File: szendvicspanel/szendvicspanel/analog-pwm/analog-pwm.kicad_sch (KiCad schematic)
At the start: 24 parts, among them J3 Conn_01x04_Pin, U1 TL072, U2 TL072

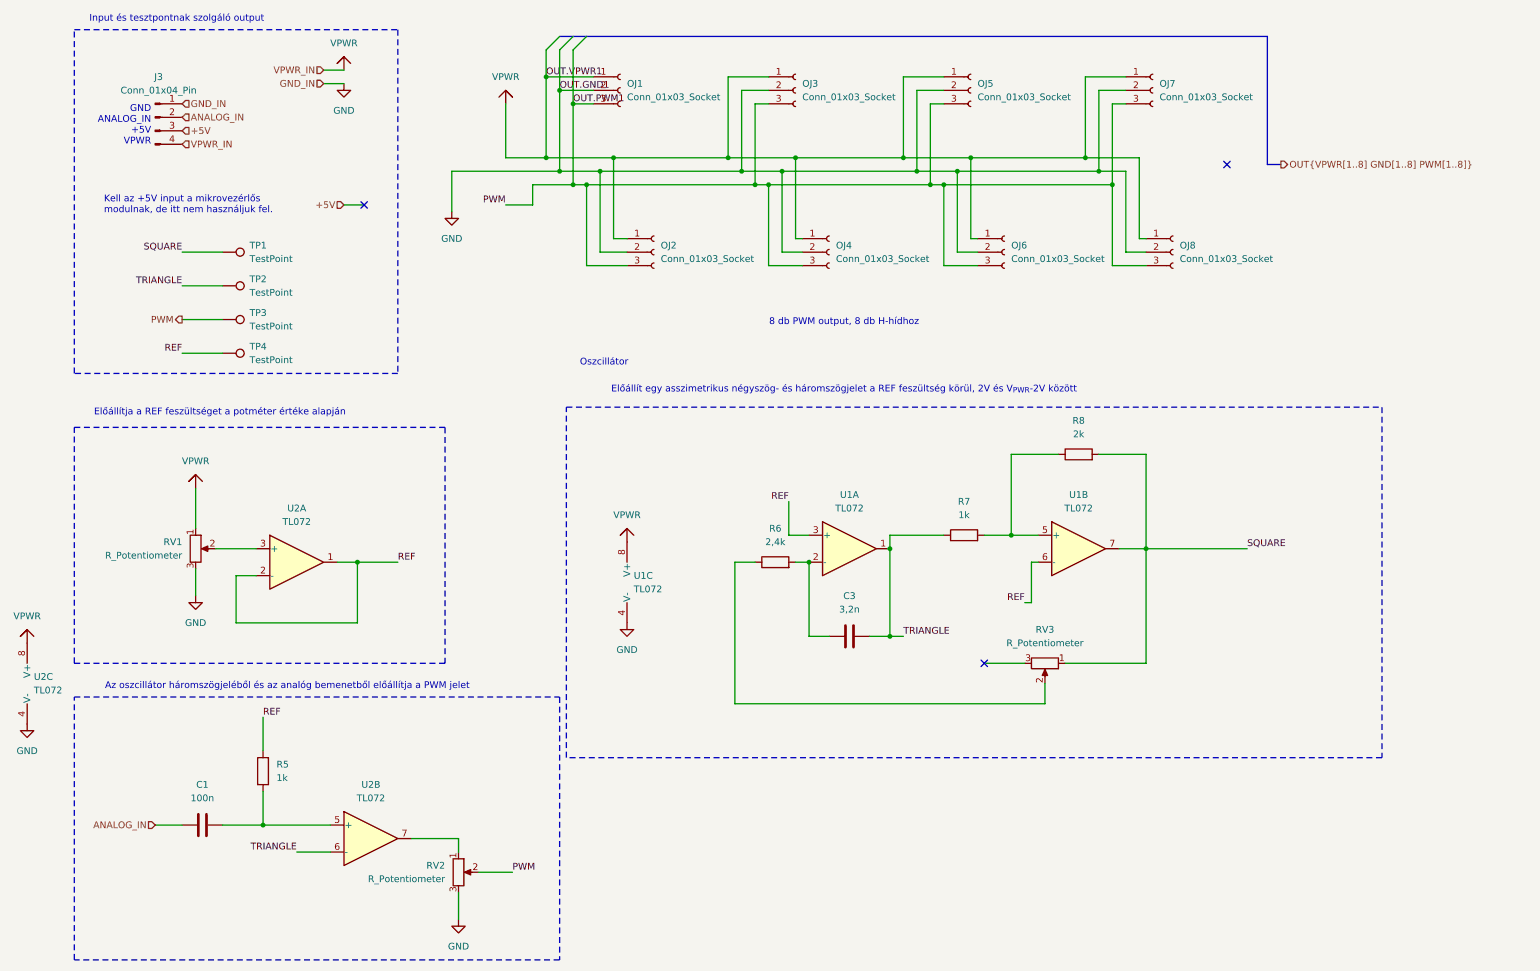
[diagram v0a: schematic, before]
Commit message: Átstrukturálás hierarchikus PCB-hez
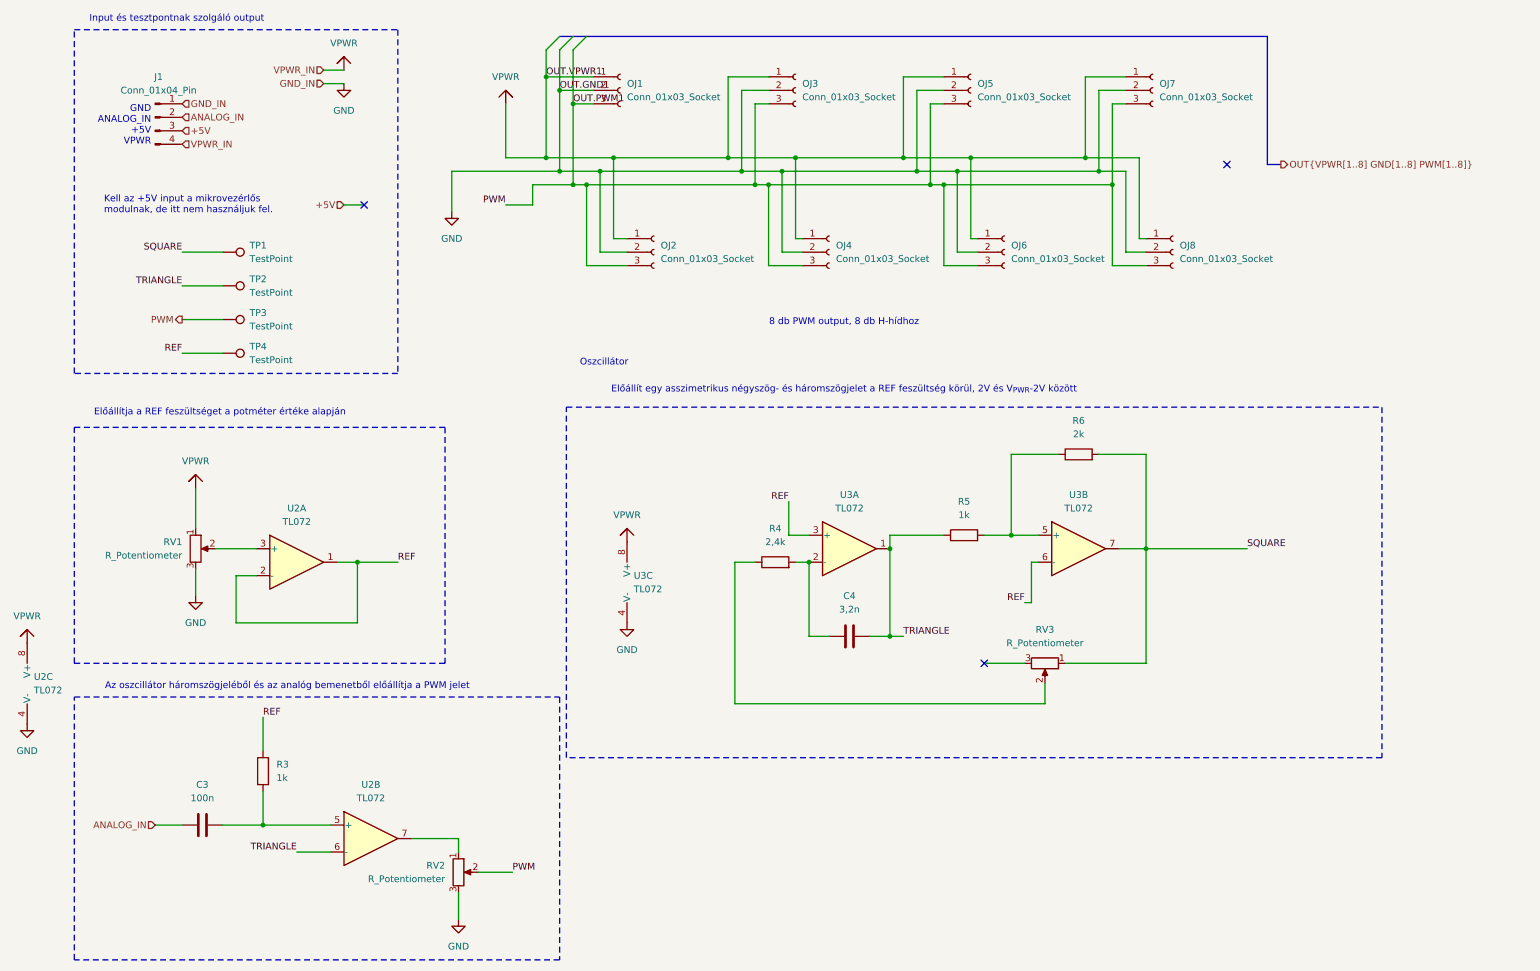
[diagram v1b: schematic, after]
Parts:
- renumbered C1 to C3, C3 to C4, J3 to J1, R5 to R3, R6 to R4, R7 to R5, R8 to R6, U1 to U3
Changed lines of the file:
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@@
 		(dnp no)
 		(fields_autoplaced yes)
-		(property "Reference" "#VPWR06"
+		(property "Reference" "#VPWR03"
 			(at 81.28 30.48 0)
 			(effects
@@
 			(project "szendvicspanel"
 				(path "/2e536be4-7a69-4064-ab31-c73232c2dcfe/2931c1ad-d139-4f81-b248-365d50218096"
-					(reference "#VPWR06")
+					(reference "#VPWR03")
 					(unit 1)
 				)
@@
 		(dnp no)
 		(fields_autoplaced yes)
-		(property "Reference" "R7"
+		(property "Reference" "R5"
 			(at 198.12 111.76 90)
 			(effects
@@
 			(project "szendvicspanel"
 				(path "/2e536be4-7a69-4064-ab31-c73232c2dcfe/2931c1ad-d139-4f81-b248-365d50218096"
-					(reference "R7")
+					(reference "R5")
 					(unit 1)
 				)
@@
 		(dnp no)
 		(fields_autoplaced yes)
-		(property "Reference" "R6"
+		(property "Reference" "R4"
 			(at 162.56 116.84 90)
 			(effects
@@
 			(project "szendvicspanel"
 				(path "/2e536be4-7a69-4064-ab31-c73232c2dcfe/2931c1ad-d139-4f81-b248-365d50218096"
-					(reference "R6")
+					(reference "R4")
 					(unit 1)
 				)
@@
 		(dnp no)
 		(fields_autoplaced yes)
-		(property "Reference" "#PWR08"
+		(property "Reference" "#PWR012"
 			(at 21.59 160.02 0)
 			(effects
@@
 			(project "szendvicspanel"
 				(path "/2e536be4-7a69-4064-ab31-c73232c2dcfe/2931c1ad-d139-4f81-b248-365d50218096"
-					(reference "#PWR08")
+					(reference "#PWR012")
 					(unit 1)
 				)
@@
 		(dnp no)
 		(fields_autoplaced yes)
-		(property "Reference" "U1"
+		(property "Reference" "U3"
 			(at 219.71 110.49 0)
 			(effects
@@
 			(project ""
 				(path "/2e536be4-7a69-4064-ab31-c73232c2dcfe/2931c1ad-d139-4f81-b248-365d50218096"
-					(reference "U1")
+					(reference "U3")
 					(unit 2)
 				)
@@
 		(dnp no)
 		(fields_autoplaced yes)
-		(property "Reference" "C3"
+		(property "Reference" "C4"
 			(at 176.53 129.54 90)
 			(effects
@@
 			(project "szendvicspanel"
 				(path "/2e536be4-7a69-4064-ab31-c73232c2dcfe/2931c1ad-d139-4f81-b248-365d50218096"
-					(reference "C3")
+					(reference "C4")
 					(unit 1)
 				)
@@
 		(dnp no)
 		(fields_autoplaced yes)
-		(property "Reference" "#PWR013"
+		(property "Reference" "#PWR015"
 			(at 101.6 63.5 0)
 			(effects
@@
 			(project "szendvicspanel"
 				(path "/2e536be4-7a69-4064-ab31-c73232c2dcfe/2931c1ad-d139-4f81-b248-365d50218096"
-					(reference "#PWR013")
+					(reference "#PWR015")
 					(unit 1)
 				)
@@
 		(dnp no)
 		(fields_autoplaced yes)
-		(property "Reference" "#PWR09"
+		(property "Reference" "#PWR013"
 			(at 53.34 135.89 0)
 			(effects
@@
 			(project "szendvicspanel"
 				(path "/2e536be4-7a69-4064-ab31-c73232c2dcfe/2931c1ad-d139-4f81-b248-365d50218096"
-					(reference "#PWR09")
+					(reference "#PWR013")
 					(unit 1)
 				)
@@
 		(dnp no)
 		(fields_autoplaced yes)
-		(property "Reference" "U1"
+		(property "Reference" "U3"
 			(at 135.89 125.7299 0)
 			(effects
@@
 			(project ""
 				(path "/2e536be4-7a69-4064-ab31-c73232c2dcfe/2931c1ad-d139-4f81-b248-365d50218096"
-					(reference "U1")
+					(reference "U3")
 					(unit 3)
 				)
@@
 		(dnp no)
 		(fields_autoplaced yes)
-		(property "Reference" "R5"
+		(property "Reference" "R3"
 			(at 68.58 161.2899 0)
 			(effects
@@
 			(project "szendvicspanel"
 				(path "/2e536be4-7a69-4064-ab31-c73232c2dcfe/2931c1ad-d139-4f81-b248-365d50218096"
-					(reference "R5")
+					(reference "R3")
 					(unit 1)
 				)
@@
 		(dnp no)
 		(fields_autoplaced yes)
-		(property "Reference" "#PWR018"
+		(property "Reference" "#PWR014"
 			(at 81.28 39.37 0)
 			(effects
@@
 			(project "szendvicspanel"
 				(path "/2e536be4-7a69-4064-ab31-c73232c2dcfe/2931c1ad-d139-4f81-b248-365d50218096"
-					(reference "#PWR018")
+					(reference "#PWR014")
 					(unit 1)
 				)
@@
 		(dnp no)
 		(fields_autoplaced yes)
-		(property "Reference" "C1"
+		(property "Reference" "C3"
 			(at 54.61 165.1 90)
 			(effects
@@
 			(project "szendvicspanel"
 				(path "/2e536be4-7a69-4064-ab31-c73232c2dcfe/2931c1ad-d139-4f81-b248-365d50218096"
-					(reference "C1")
+					(reference "C3")
 					(unit 1)
 				)
@@
 		(dnp no)
 		(fields_autoplaced yes)
-		(property "Reference" "J3"
+		(property "Reference" "J1"
 			(at 46.355 31.75 0)
 			(effects
@@
 			(project "szendvicspanel"
 				(path "/2e536be4-7a69-4064-ab31-c73232c2dcfe/2931c1ad-d139-4f81-b248-365d50218096"
-					(reference "J3")
+					(reference "J1")
 					(unit 1)
 				)
@@
 		(dnp no)
 		(fields_autoplaced yes)
-		(property "Reference" "U1"
+		(property "Reference" "U3"
 			(at 176.53 110.49 0)
 			(effects
@@
 			(project ""
 				(path "/2e536be4-7a69-4064-ab31-c73232c2dcfe/2931c1ad-d139-4f81-b248-365d50218096"
-					(reference "U1")
+					(reference "U3")
 					(unit 1)
 				)
@@
 		(dnp no)
 		(fields_autoplaced yes)
-		(property "Reference" "R8"
+		(property "Reference" "R6"
 			(at 219.71 96.52 90)
 			(effects
@@
 			(project "szendvicspanel"
 				(path "/2e536be4-7a69-4064-ab31-c73232c2dcfe/2931c1ad-d139-4f81-b248-365d50218096"
-					(reference "R8")
-					(unit 1)
-				)
+					(reference "R6")
+					(unit 1)
+				)
